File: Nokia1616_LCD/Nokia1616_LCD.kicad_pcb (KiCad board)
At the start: 2 copper layers, 35.1 x 54.4 mm, 3 parts, among them P1 CONN_01X08

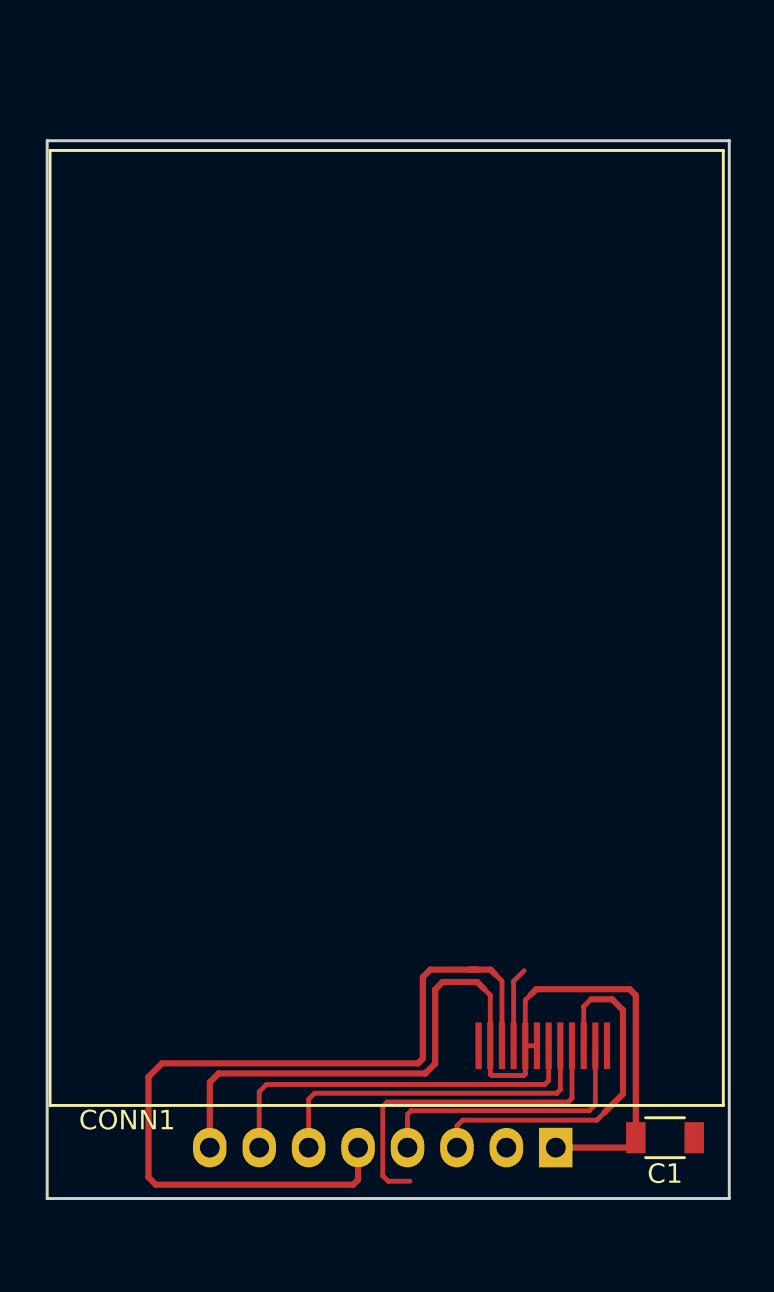
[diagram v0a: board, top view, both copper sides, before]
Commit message: Changed Nokia1616 LCD backlight Added a low switch NPN transistor for PWM switching of backlight to ground Added a capacitor to ground on the 3v3 line Cleaned up the traces a bit
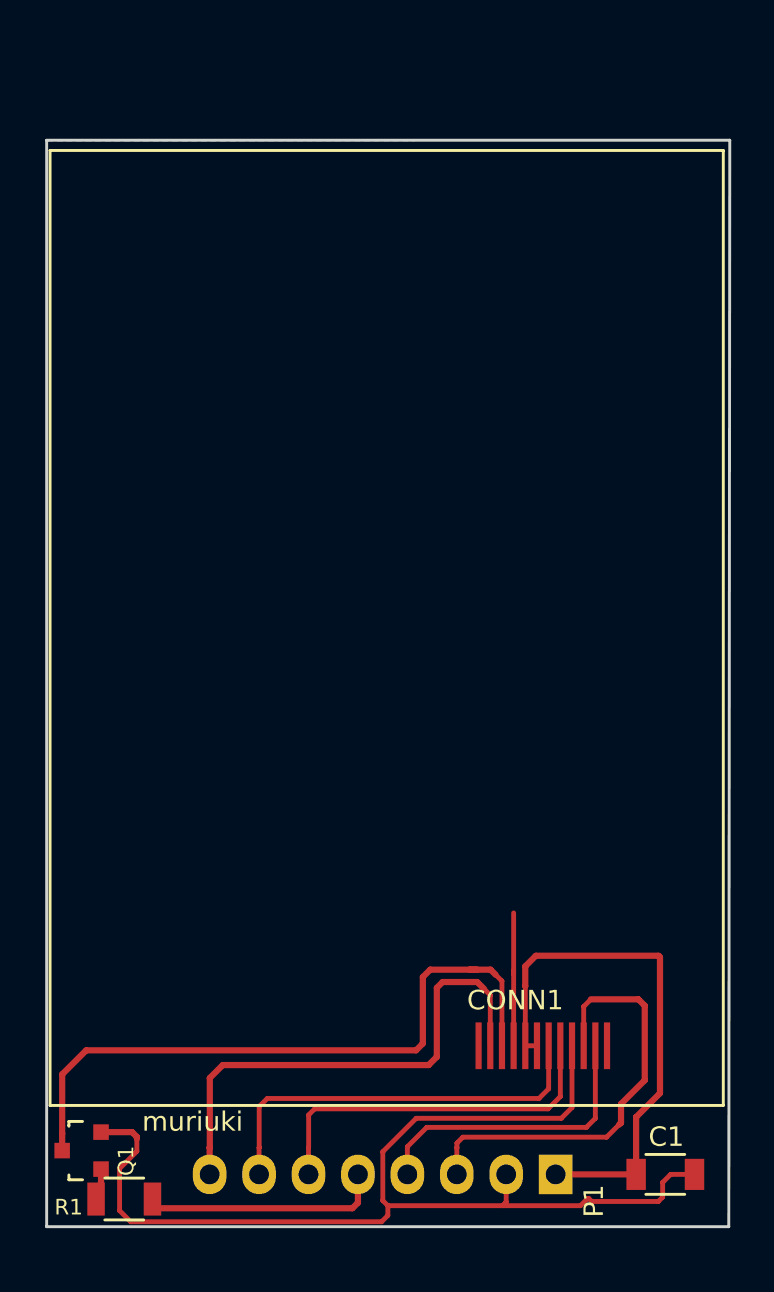
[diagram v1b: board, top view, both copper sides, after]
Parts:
- added Q1: BC547_BEC_123, TO_SOT_Packages_SMD:SOT-23, F.Cu at (56.7, 121.8)
- added R1: 1K, Resistors_SMD:R_1206, F.Cu at (58.9, 124.3)
- CONN1: footprint Nokia1616_LCD -> Connect:Nokia1616_LCD
- moved C1 1.88 mm to (86.7, 123.0)
- moved P1 1.38 mm to (81.0, 123.0)
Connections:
- CONN1 pad 10: LED -> LED-
- CONN1 pad 11: VCC -> 5V
- P1 pad 8: VCC -> 5V
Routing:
- net GND: track 21.8 -> 63.2 mm
- net LED-: track 0.00 -> 34.7 mm
- net LED: track 44.7 -> 12.3 mm
- net 5V: track 0.00 -> 26.4 mm
- net VCC: track 50.7 -> 27.7 mm
- net CE: track 19.1 -> 22.4 mm
- net Net-(Q1-Pad1): track 0.00 -> 1.64 mm
- net CLK: track 19.8 -> 21.0 mm
- net MOSI: track 17.9 -> 19.0 mm
- net RESET: track 14.6 -> 15.3 mm
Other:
- board size 35.1 x 54.4 mm -> 35.1 x 55.8 mm
- net class Default: trace_width 0.25 -> 0.32
- board text added: "muriuki"

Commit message: Added Simulation Circuits and POV board
Added a BJT characteristics simulation circuit
Add a Voltage Divider simulation circuit
Add an amplifier simulation circuit
Add a Nokia LCD breakout board
Add a POV LED MKL05Z board
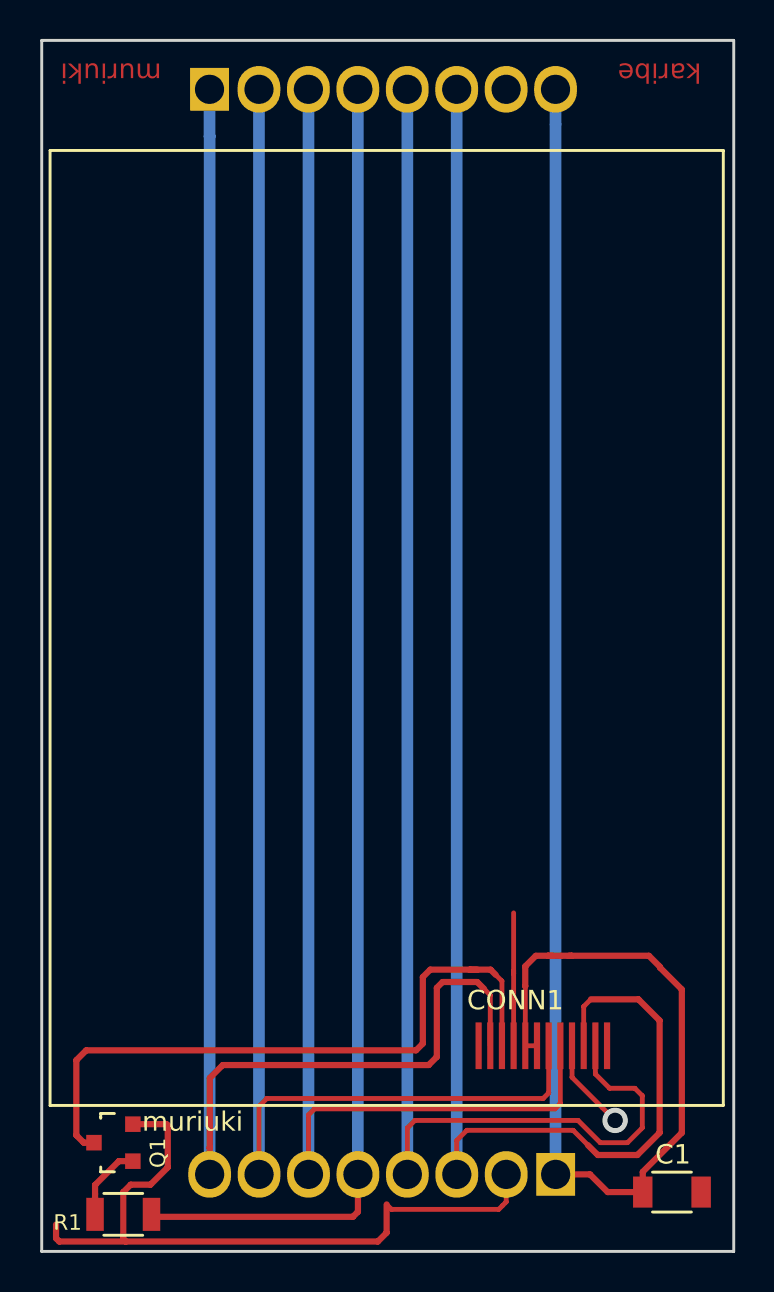
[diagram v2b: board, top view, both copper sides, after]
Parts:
- added P2: CONN_01X08, Connect:Pin_Header_Straight_1x08_Rivet2, B.Cu at (63.2, 67.3)
- P1: footprint Pin_Headers:Pin_Header_Straight_1x08 -> Connect:Pin_Header_Straight_1x08_Rivet2
- moved Q1 1.69 mm to (58.3, 121.4)
- moved C1 0.97 mm to (87.0, 124.0)
- moved R1 0.79 mm to (58.8, 125.1)
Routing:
- net RESET: track 15.3 -> 77.4 mm
- net CE: track 22.4 -> 82.0 mm
- net VCC: track 27.7 -> 86.0 mm
- net LED: track 12.3 -> 68.8 mm
- net MOSI: track 19.0 -> 75.3 mm
- net CLK: track 21.0 -> 77.2 mm
- net 5V: track 26.4 -> 82.1 mm
- net GND: track 63.2 -> 48.4 mm, vias 0 -> 1
- net Net-(Q1-Pad1): track 1.64 -> 4.09 mm
- added copper zone on B.Cu, net GND
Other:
- board size 35.1 x 55.8 mm -> 35.6 x 62.2 mm
- net class Default: trace_width 0.32 -> 0.6
- board text added: "karibe"

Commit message: Too many untracked changes: LCD boards update and switch to KiCAD version 5
Update the Nokia LCD breakout boards
Add more KiCAD simulation projects
Update most projects to KiCAD version 5
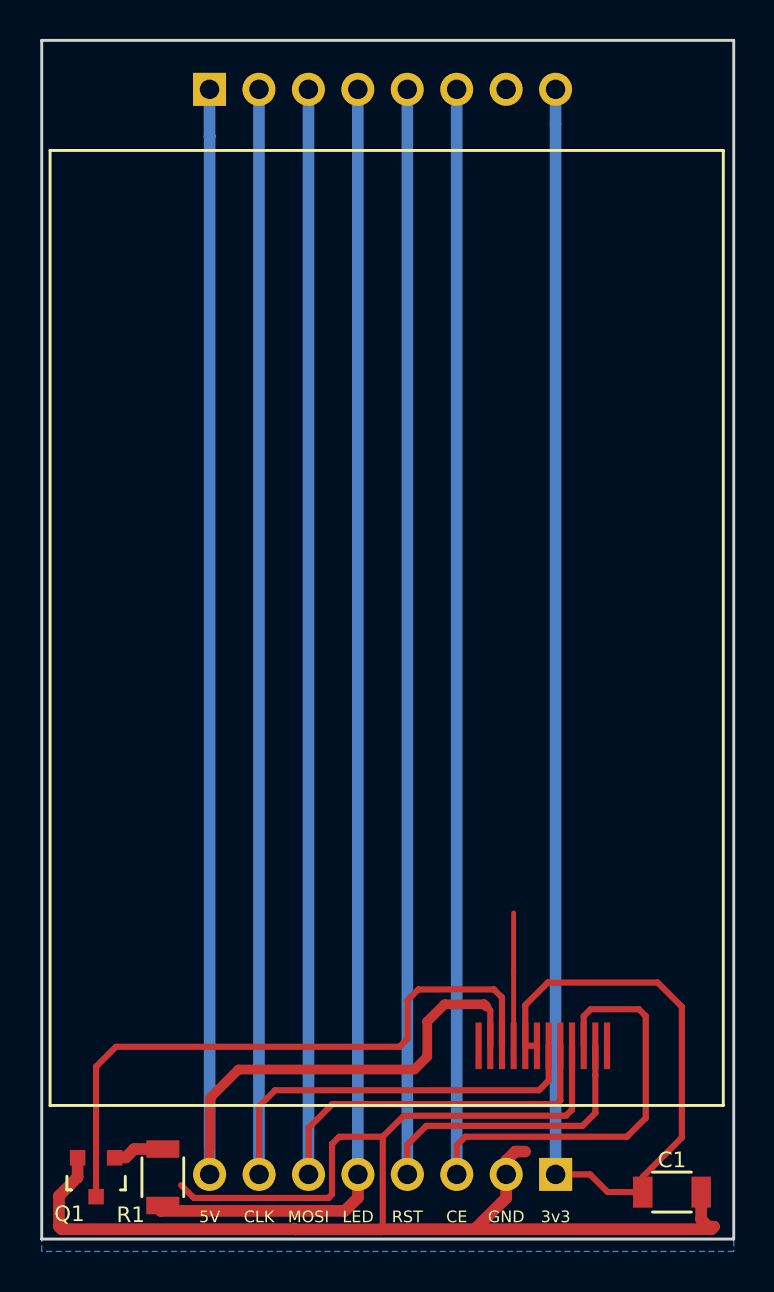
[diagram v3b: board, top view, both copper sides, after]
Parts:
- P1, P2: footprint Connect:Pin_Header_Straight_1x08_Rivet2 -> Pin_Headers:Pin_Header_Straight_1x08_Pitch2.54mm
- moved R1 2.79 mm to (60.8, 123.2), turned to 270 degrees
- moved Q1 1.99 mm to (57.4, 123.2), turned to 180 degrees
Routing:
- net GND: track 48.4 -> 84.1 mm, vias 1 -> 0
- net RESET: track 77.4 -> 71.3 mm
- net CE: track 82.0 -> 78.3 mm
- net VCC: track 86.0 -> 82.7 mm
- net 5V: track 82.1 -> 79.1 mm
- net LED-: track 34.7 -> 33.0 mm
- net Net-(Q1-Pad1): track 4.09 -> 2.67 mm
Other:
- board size 35.6 x 62.2 mm -> 35.6 x 61.6 mm
- rule pad_to_mask_clearance: 0.2 -> 0.0762
- board text added: "3v3"
- board text added: "5V"
- board text added: "CE"
- board text added: "CLK"
- board text added: "GND"
- board text added: "Karibe (K) Ltd karibe.co.ke"
- board text added: "LED"
- board text added: "MOSI"
- board text added: "RST"
- board text removed: "karibe"
- board text removed: "muriuki"
